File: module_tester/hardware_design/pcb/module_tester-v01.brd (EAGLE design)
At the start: 198.1 x 116.8 mm, 110 parts, among them IC1 LM4040 4.1V, IC2 TL074P, IC3 MCP4822, IC4 ATMEGA644p, IC5 74HC595N, IC6 74HC165N, IC7 MCP6002, J1 PJ301WQP, J10 PJ301WQP, J11 PJ301WQP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

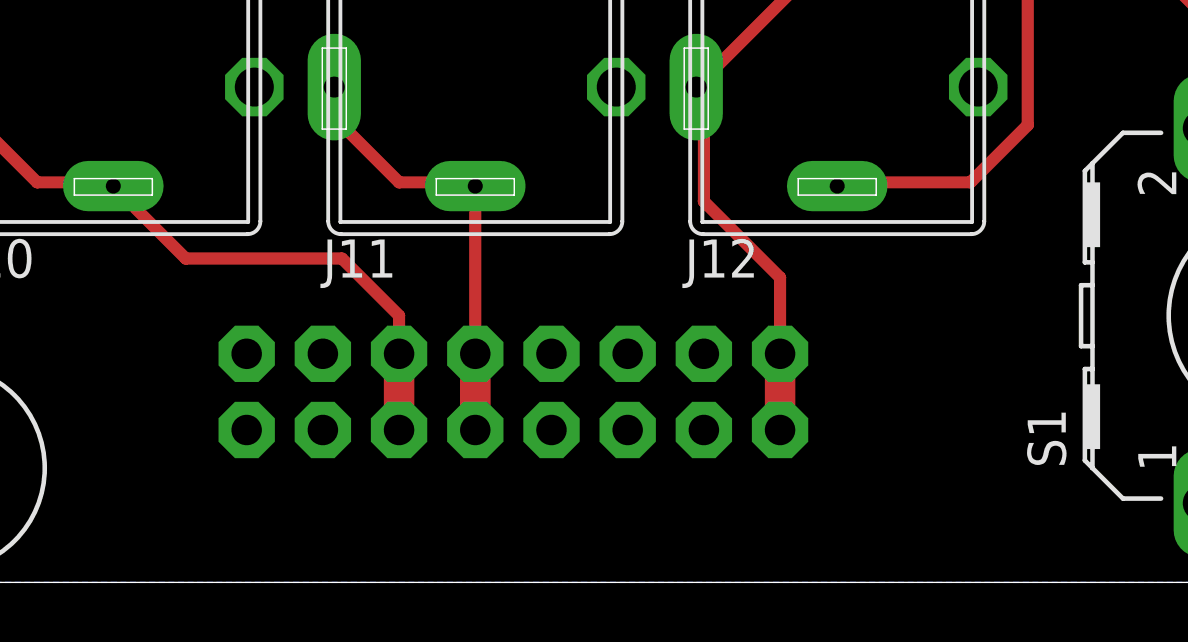
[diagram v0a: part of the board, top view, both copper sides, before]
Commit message: DCDC Converter and Ammeter Jacks
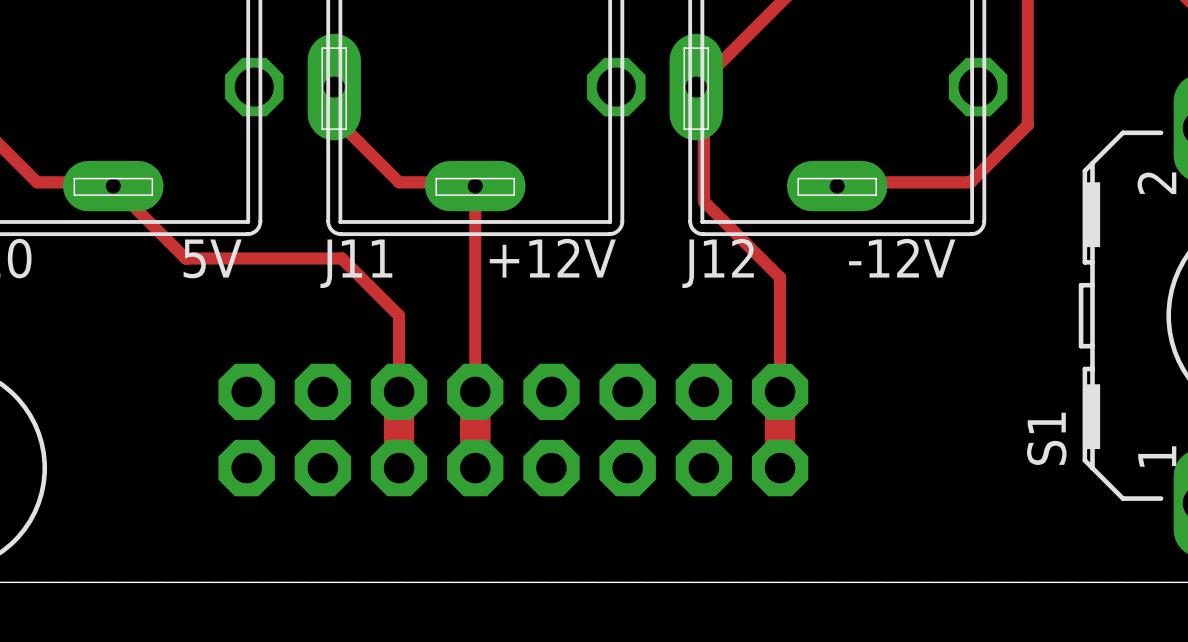
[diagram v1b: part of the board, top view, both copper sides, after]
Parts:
- moved J7 1.27 mm to (14.0, 6.35)
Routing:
- net N$22: track 19.3 -> 20.6 mm
- net N$10: track 14.8 -> 16.1 mm
- net N$8: track 21.8 -> 23.1 mm
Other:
- board text added: "+12V"
- board text added: "-12V"
- board text added: "5V"
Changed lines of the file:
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@@
 <wire x1="194.31" y1="0" x2="198.12" y2="3.81" width="0" layer="20" curve="89.996992"/>
 <wire x1="198.12" y1="3.81" x2="198.12" y2="113.03" width="0" layer="20"/>
-<wire x1="11.43" y1="10.16" x2="11.43" y2="2.54" width="0.4064" layer="26"/>
-<wire x1="11.43" y1="2.54" x2="34.29" y2="2.54" width="0.4064" layer="26"/>
-<wire x1="34.29" y1="2.54" x2="34.29" y2="10.16" width="0.4064" layer="26"/>
-<wire x1="34.29" y1="10.16" x2="11.43" y2="10.16" width="0.4064" layer="26"/>
+<wire x1="11.43" y1="8.89" x2="11.43" y2="1.27" width="0.4064" layer="26"/>
+<wire x1="11.43" y1="1.27" x2="34.29" y2="1.27" width="0.4064" layer="26"/>
+<wire x1="34.29" y1="1.27" x2="34.29" y2="8.89" width="0.4064" layer="26"/>
+<wire x1="34.29" y1="8.89" x2="11.43" y2="8.89" width="0.4064" layer="26"/>
 <wire x1="184.785" y1="43.815" x2="184.785" y2="34.925" width="0.254" layer="21"/>
 <wire x1="184.785" y1="34.925" x2="191.135" y2="34.925" width="0.254" layer="21"/>
@@
 <vertex x="1.27" y="28.575"/>
 </polygon>
+<text x="11.7475" y="10.16" size="1.27" layer="25" ratio="15">5V</text>
+<text x="21.9075" y="10.16" size="1.27" layer="25" ratio="15">+12V</text>
+<text x="33.9725" y="10.16" size="1.27" layer="25" ratio="15">-12V</text>
 </plain>
 <attributes>
@@
 <attribute name="VALUE" x="172.974" y="18.796" size="0.8128" layer="27" ratio="10"/>
 </element>
-<element name="J7" library="og-header" package="2X8" value="M08X2" x="13.97" y="7.62" smashed="yes" rot="MR180">
-<attribute name="NAME" x="11.43" y="1.905" size="1.27" layer="26" ratio="10" rot="MR180"/>
+<element name="J7" library="og-header" package="2X8" value="M08X2" x="13.97" y="6.35" smashed="yes" rot="MR180">
+<attribute name="NAME" x="8.255" y="2.54" size="1.27" layer="26" ratio="10" rot="MR180"/>
 </element>
 <element name="R6" library="rcl" package="0204/7" value="10k" x="167.64" y="106.045" smashed="yes">
@@
 <contactref element="J7" pad="6"/>
 <contactref element="J7" pad="5"/>
-<wire x1="19.05" y1="7.62" x2="19.05" y2="5.08" width="1.016" layer="1"/>
+<wire x1="19.05" y1="6.35" x2="19.05" y2="3.81" width="1.016" layer="1"/>
 <contactref element="J10" pad="SW"/>
 <contactref element="J10" pad="GND"/>
-<wire x1="19.05" y1="7.62" x2="19.05" y2="8.89" width="0.4064" layer="1"/>
+<wire x1="19.05" y1="6.35" x2="19.05" y2="8.89" width="0.4064" layer="1"/>
 <wire x1="19.05" y1="8.89" x2="17.145" y2="10.795" width="0.4064" layer="1"/>
 <wire x1="17.145" y1="10.795" x2="11.94" y2="10.795" width="0.4064" layer="1"/>
@@
 <contactref element="J7" pad="8"/>
 <contactref element="J7" pad="7"/>
-<wire x1="21.59" y1="5.08" x2="21.59" y2="7.62" width="1.016" layer="1"/>
+<wire x1="21.59" y1="3.81" x2="21.59" y2="6.35" width="1.016" layer="1"/>
 <contactref element="J11" pad="SW"/>
 <contactref element="J11" pad="GND"/>
@@
 <wire x1="19.05" y1="13.335" x2="21.465" y2="13.335" width="0.4064" layer="1"/>
 <wire x1="21.465" y1="13.335" x2="21.59" y2="13.21" width="0.4064" layer="1"/>
-<wire x1="21.59" y1="13.21" x2="21.59" y2="7.62" width="0.4064" layer="1"/>
+<wire x1="21.59" y1="13.21" x2="21.59" y2="6.35" width="0.4064" layer="1"/>
 </signal>
 <signal name="N$22">
 <contactref element="J7" pad="16"/>
 <contactref element="J7" pad="15"/>
-<wire x1="31.75" y1="7.62" x2="31.75" y2="5.08" width="1.016" layer="1"/>
+<wire x1="31.75" y1="6.35" x2="31.75" y2="3.81" width="1.016" layer="1"/>
 <contactref element="J12" pad="TIP"/>
 <contactref element="J12" pad="GND"/>
-<wire x1="31.75" y1="7.62" x2="31.75" y2="10.16" width="0.4064" layer="1"/>
+<wire x1="31.75" y1="6.35" x2="31.75" y2="10.16" width="0.4064" layer="1"/>
 <wire x1="31.75" y1="10.16" x2="29.21" y2="12.7" width="0.4064" layer="1"/>
 <wire x1="29.21" y1="12.7" x2="29.21" y2="16.255" width="0.4064" layer="1"/>
